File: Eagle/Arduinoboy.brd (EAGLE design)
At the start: 68.6 x 53.3 mm, 22 parts

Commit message: Update eagle designs
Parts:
- moved STATUS 34.3 mm to (30.8, 11.1), turned to 0 degrees
- moved OK1 29.5 mm to (36.7, 39.7)
- moved R1 8.98 mm to (19.4, 42.4)
- moved R2 8.98 mm to (16.8, 42.4)
- moved R4 8.98 mm to (24.5, 42.4)
- moved R5 8.98 mm to (22.0, 42.4)
- moved R3 8.98 mm to (14.3, 42.4)
- moved R6 8.98 mm to (11.8, 42.4)
- moved D1 7.02 mm to (28.9, 40.3), turned to 270 degrees
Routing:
- net N$2: track 68.0 -> 28.2 mm
- net N$1: track 53.5 -> 15.7 mm
- net N$14: track 17.3 -> 46.8 mm, vias 0 -> 1
- net GND: track 124.6 -> 151.6 mm
- net N$5: track 36.1 -> 60.1 mm, vias 1 -> 0
- net N$9: track 74.2 -> 51.8 mm
- net N$4: track 96.4 -> 118.1 mm
- net VCC: track 59.1 -> 47.7 mm
- net N$18: track 28.2 -> 37.9 mm, vias 0 -> 1
- net N$17: track 56.4 -> 52.5 mm
- net N$22: track 58.8 -> 55.3 mm, vias 1 -> 0
- net N$13: track 40.3 -> 42.3 mm
- net N$16: track 32.2 -> 30.3 mm
- net N$24: track 47.4 -> 45.4 mm
- net N$15: track 48.9 -> 47.6 mm
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- added copper zone on layer 1, net GND
- added copper zone on layer 16, net GND
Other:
- board text added: "2"
- board text added: "4"
- board text added: "5"

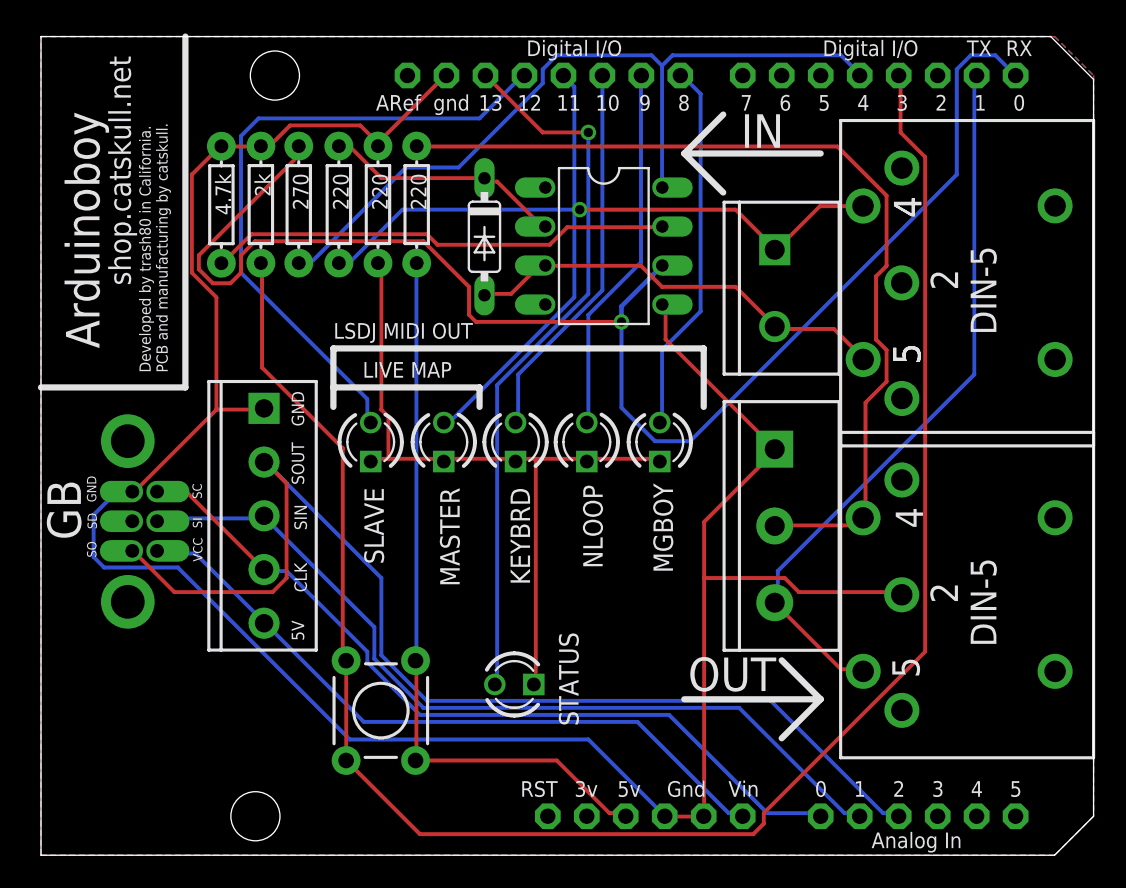
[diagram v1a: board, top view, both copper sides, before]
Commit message: Fix PCB bugs
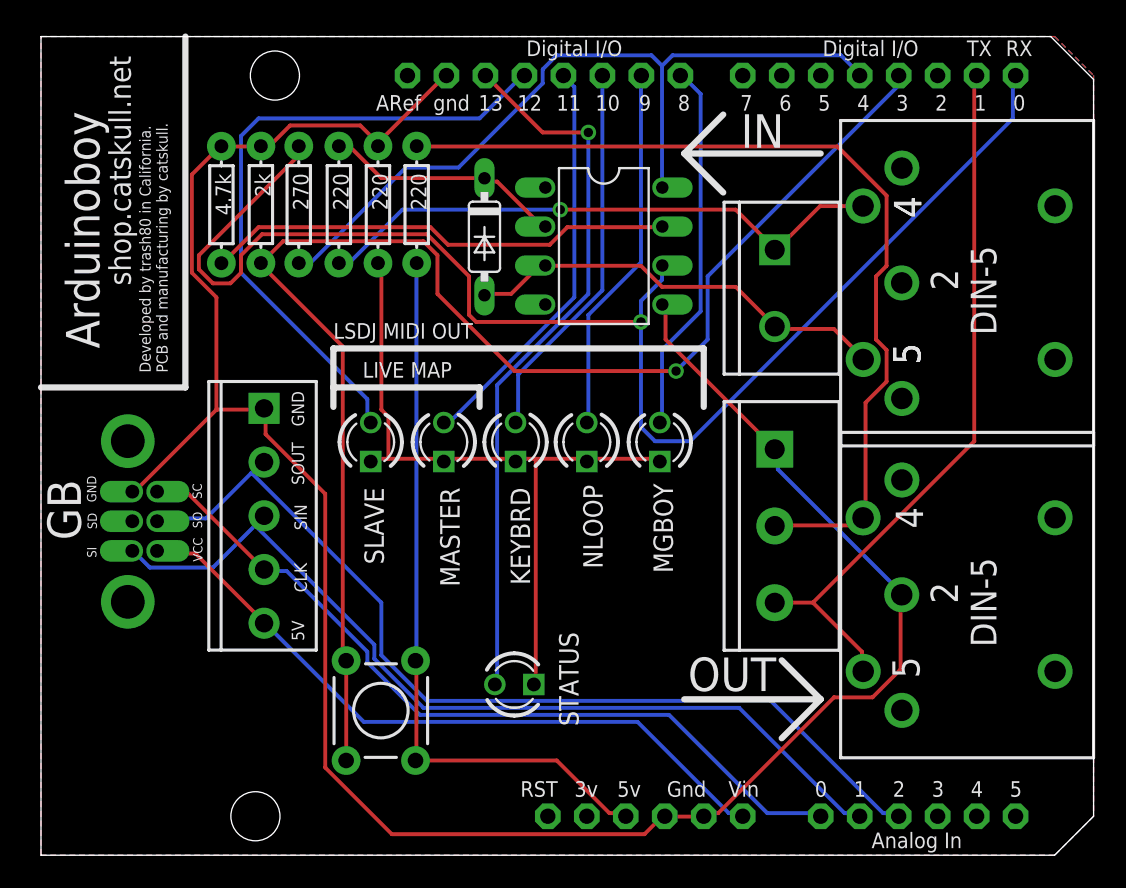
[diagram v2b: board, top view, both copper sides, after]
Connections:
- net N$22: now also U$1.SO; no longer U$1.SI
- net N$23: now also U$1.SI; no longer U$1.SO
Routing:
- net N$4: track 118.1 -> 92.6 mm, vias 0 -> 1
- net N$23: track 73.6 -> 62.0 mm
- net GND: track 151.6 -> 146.4 mm
- net N$22: track 55.3 -> 59.1 mm
- net N$10: track 95.7 -> 93.1 mm
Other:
- board text added: "1.0.1"
- board text removed: "1.0.0"

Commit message: Add eagle files for v1.1.0
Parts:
- removed JP1: (no value), SparkFun-Connectors:SCREWTERMINAL-5MM-2
- removed JP2: (no value), SparkFun-Connectors:SCREWTERMINAL-5MM-3
- removed JP3: (no value), SparkFun-Connectors:SCREWTERMINAL-3.5MM-5
- removed U$4, U$5: MIDI_CONN_FEMALE_SUPPORT, SparkFun-Connectors:DIN_5_FEMALE_SUPPORT
- added U$2, U$6: MIDI-DIN-5, MIDI by Jazz:MIDI-DIN-5
- added X1: (no value), mini_din:M_DIN6
- moved S2 14.8 mm to (7.43, 8.19)
- moved STATUS 5.68 mm to (35.9, 13.7)
- moved D1 0.83 mm to (28.1, 40.3)
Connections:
- removed net N$22: JP3.3, U$1.SO, U$3.A1
- removed net N$23: JP3.2, U$1.SI, U$3.A2
- removed net N$24: JP3.5, U$1.VCC, U$3.VIN
- new net N$19: R1.P$2, U$6.4
- new net N$20: U$1.SI, U$3.A2, X1.1
- new net N$21: U$1.SO, U$3.A1
- new net PE1: X1.SH1
- new net PE2: X1.SH2
- new net PE3: X1.SH3
- net GND: now also U$2.2, X1.3; no longer JP2.1, JP3.1, U$4.2
- net N$17: now also X1.5; no longer JP3.4
- net N$18: now also U$1.VCC, U$3.VIN; no longer JP1.1, R1.P$2, U$5.4
- net N$2: now also U$6.5; no longer JP1.2, U$5.5
- net N$5: now also U$2.4; no longer JP2.2, U$4.4
- net N$7: now also U$2.5; no longer JP2.3, U$4.5
- net VCC: now also X1.4
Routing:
- net N$19: track 0.00 -> 71.5 mm
- net N$23: track 62.0 -> 0.00 mm
- net N$22: track 59.1 -> 0.00 mm
- net N$20: track 0.00 -> 58.2 mm
- net N$21: track 0.00 -> 56.6 mm
- net N$24: track 45.4 -> 0.00 mm
- net VCC: track 47.7 -> 85.4 mm
- net N$4: track 92.6 -> 122.1 mm, vias 1 -> 0
- net N$10: track 93.1 -> 75.1 mm, vias 1 -> 0
- net GND: track 146.4 -> 131.9 mm, vias 0 -> 1
- net N$9: track 51.8 -> 65.8 mm
- net N$13: track 42.3 -> 30.3 mm
- net N$18: track 37.9 -> 45.8 mm, vias 1 -> 0
- net N$7: track 47.1 -> 41.2 mm
- net N$14: track 46.8 -> 42.9 mm, vias 1 -> 0
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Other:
- board text added: "1.1.0"
- board text added: "PS/2"
- board text removed: "1.0.1"
- board text removed: "2"
- board text removed: "4"
- board text removed: "5"
- board text removed: "5V"
- board text removed: "CLK"
- board text removed: "GND"
- board text removed: "SIN"
- board text removed: "SOUT"

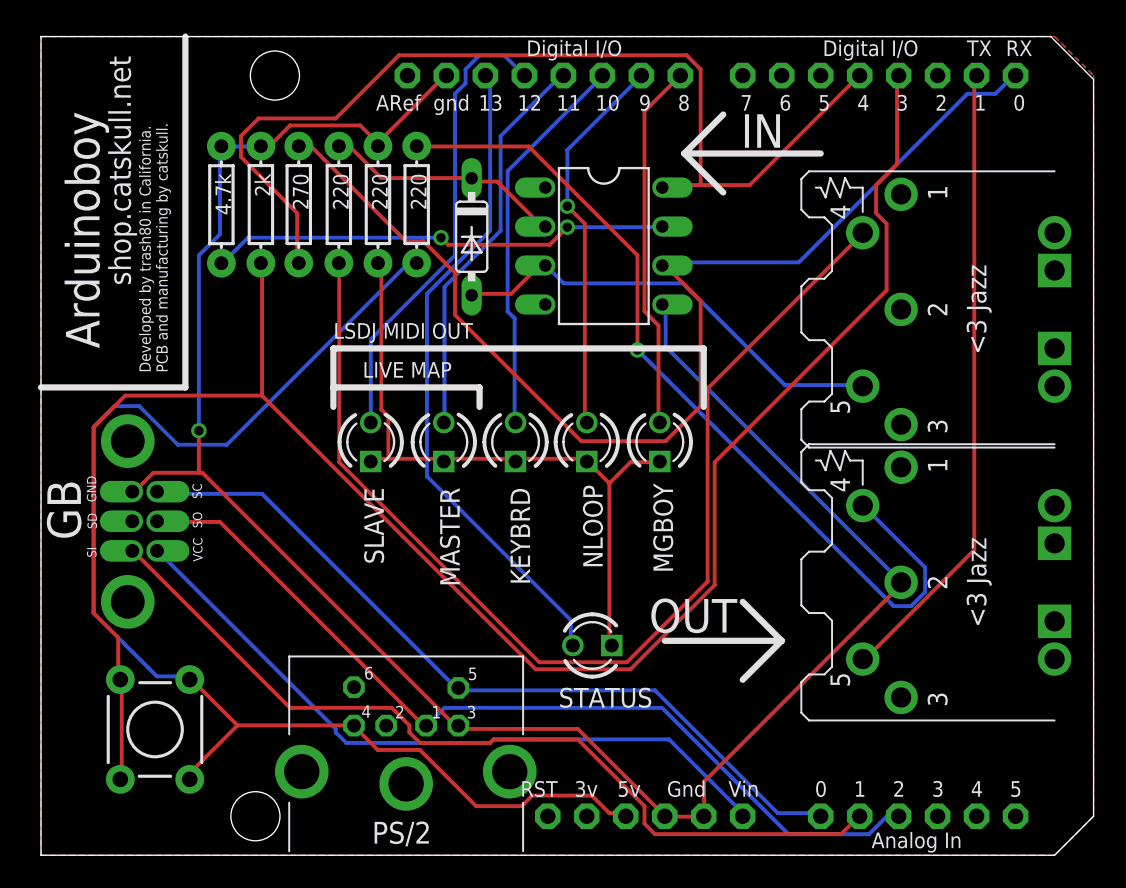
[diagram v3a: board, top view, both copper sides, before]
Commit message: Update eagle files to v1.1.1
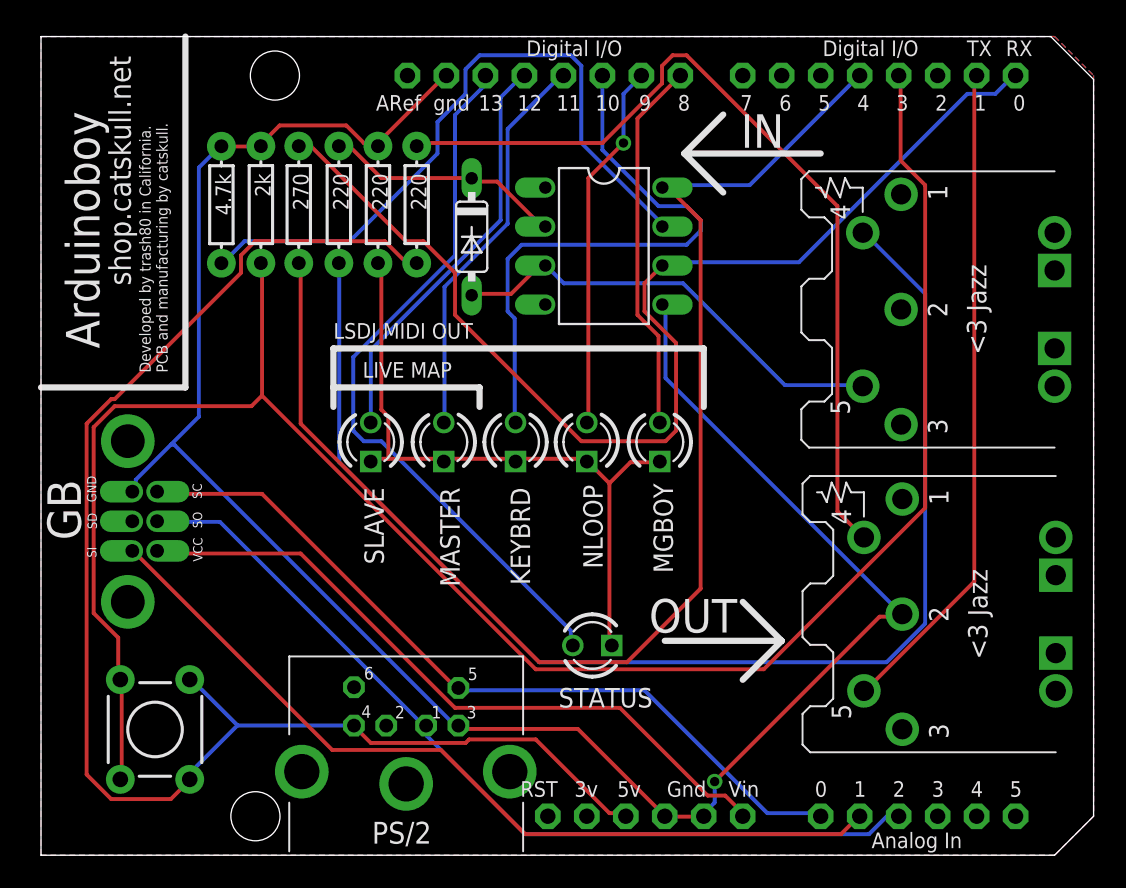
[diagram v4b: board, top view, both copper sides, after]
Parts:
- moved U$2 2.07 mm to (66.1, 15.7)
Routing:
- net N$9: track 65.8 -> 88.4 mm
- net N$16: track 30.1 -> 44.1 mm, vias 2 -> 0
- net N$19: track 71.5 -> 84.8 mm
- net N$11: track 25.4 -> 38.0 mm
- net VCC: track 85.4 -> 95.6 mm
- net N$4: track 122.1 -> 128.1 mm
- net N$14: track 42.9 -> 47.4 mm
- net N$13: track 30.3 -> 26.8 mm
- net N$7: track 41.2 -> 43.2 mm
- net GND: track 131.9 -> 133.6 mm
- net N$21: track 56.6 -> 55.5 mm
- net N$8: track 25.1 -> 24.1 mm
- net N$20: track 58.2 -> 57.6 mm
- net N$5: vias 1 -> 0
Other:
- board text added: "1.1.1"
- board text removed: "1.1.0"

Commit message: Update eagle files
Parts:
- renumbered KEYBRD to KB, MGBOY to MGB, NLOOP to NL
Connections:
- removed net N$20: U$1.SI, U$3.A2, X1.1
- new net N$22: U$1.SI, U$3.A2
- net N$21: now also X1.1
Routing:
- net N$22: track 0.00 -> 58.1 mm
- net N$20: track 57.6 -> 0.00 mm
- net N$9: track 88.4 -> 44.0 mm, vias 0 -> 2
- net VCC: track 95.6 -> 70.4 mm, vias 0 -> 1
- net N$8: track 24.1 -> 43.7 mm
- net GND: track 133.6 -> 141.7 mm, vias 1 -> 12
- net N$19: track 84.8 -> 78.9 mm
- net N$18: track 45.4 -> 48.3 mm
- net N$21: track 55.5 -> 57.1 mm
- net N$17: track 52.1 -> 52.8 mm
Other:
- board text added: "1.1.3"
- board text removed: "1.1.1"
